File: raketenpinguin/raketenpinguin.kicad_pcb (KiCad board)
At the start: 2 copper layers, 44.3 x 88 mm, 6 parts, among them J101 Conn_01x01_Male, J102 Conn_01x01_Male

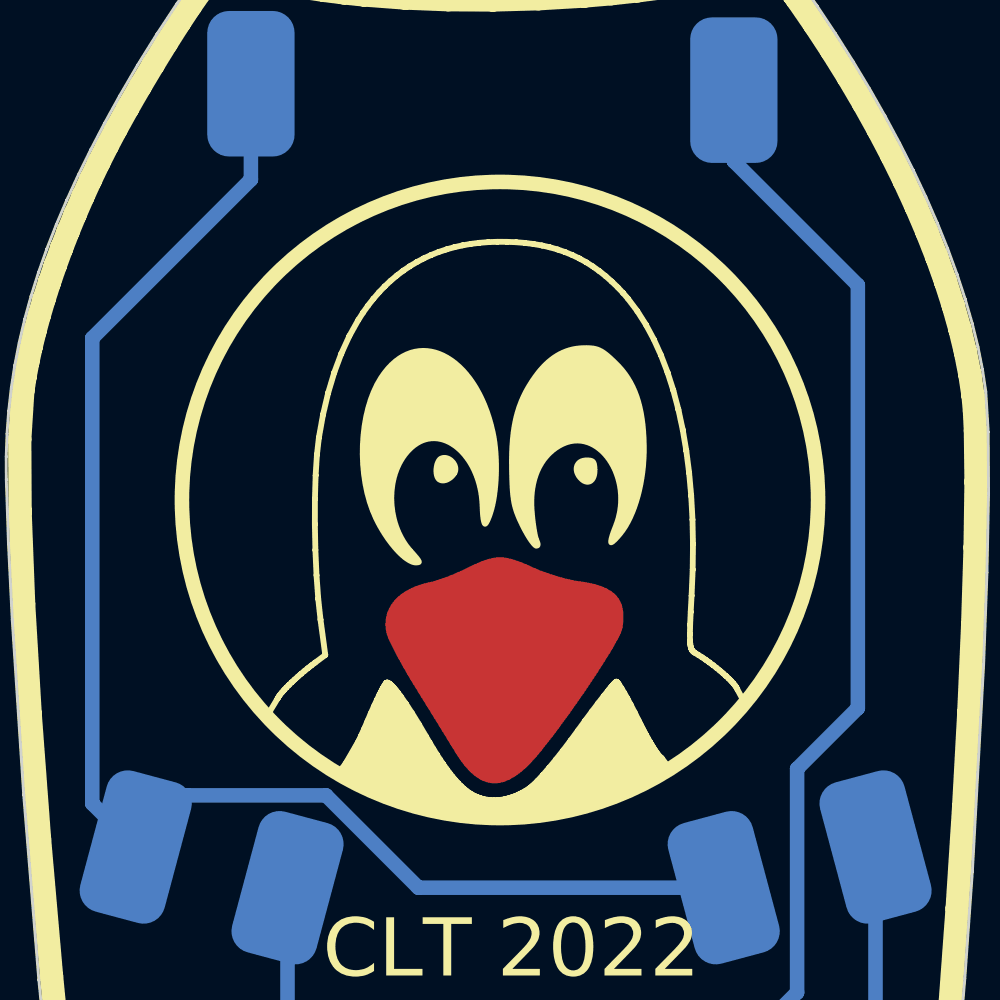
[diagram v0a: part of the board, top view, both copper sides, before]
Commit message: Raketenpinguin: Add Cu behind head
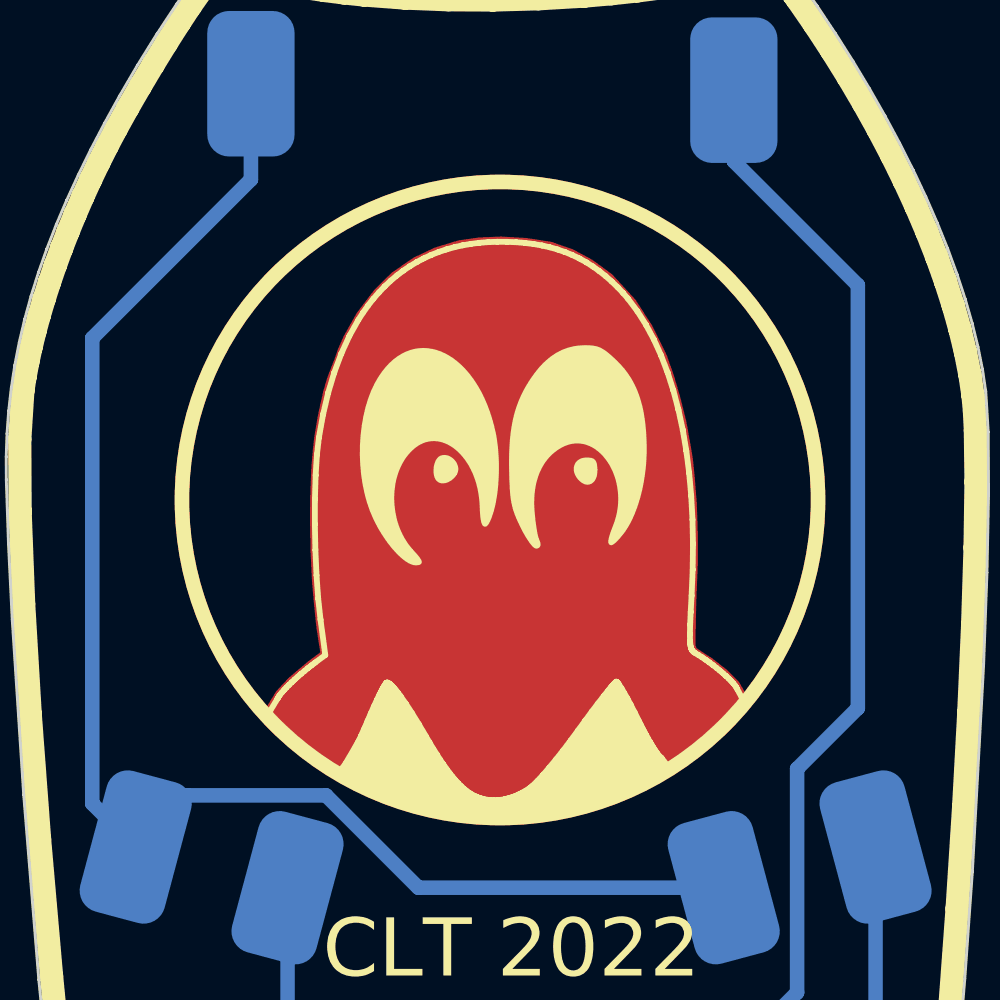
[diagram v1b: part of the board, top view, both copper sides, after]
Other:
- board text added: "Logo: Chemnitzer Linuxtage Design: CC-BY-SA Chrissi^ https://gitli.stratum0.org/chrissi/clt-soldering V2"
- board text removed: "Logo: Chemnitzer Linuxtage Design: CC-BY-SA Chrissi^ https://gitli.stratum0.org/chrissi/clt-soldering"
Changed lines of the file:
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@@
     (48 "B.Fab" user)
     (49 "F.Fab" user)
-    (50 "User.1" user)
-    (51 "User.2" user)
-    (52 "User.3" user)
-    (53 "User.4" user)
-    (54 "User.5" user)
-    (55 "User.6" user)
-    (56 "User.7" user)
-    (57 "User.8" user)
-    (58 "User.9" user)
+    (50 "User.1" user "Nutzer.1")
+    (51 "User.2" user "Nutzer.2")
+    (52 "User.3" user "Nutzer.3")
+    (53 "User.4" user "Nutzer.4")
+    (54 "User.5" user "Nutzer.5")
+    (55 "User.6" user "Nutzer.6")
+    (56 "User.7" user "Nutzer.7")
+    (57 "User.8" user "Nutzer.8")
+    (58 "User.9" user "Nutzer.9")
   )
   (setup
@@
     )
     (pad_to_mask_clearance 0)
-    (grid_origin 101.69 51.08)
+    (grid_origin 90.27 57.12)
     (pcbplotparams
       (layerselection 0x00010fc_ffffffff)
@@
       (drillshape 0)
       (scaleselection 1)
-      (outputdirectory "V1/drill/")
+      (outputdirectory "V2/drill")
     )
   )
@@
       (net 4 "/GND") (pintype "passive"))
   )
+  (gr_circle (center 79.096742 57.26) (end 90.023484 57.26) (layer "F.Cu") (width 0.5) (fill none))
   (gr_poly
     (pts
@@
       (xy 80.058218 66.301112)
     ) (layer "F.Cu") (width 0.126504) (fill solid))
+  (gr_poly
+    (pts
+      (xy 80 48.36)
+      (xy 80.84 48.49)
+      (xy 81.56 48.74)
+      (xy 82.21 49.09)
+      (xy 82.88 49.58)
+      (xy 83.68 50.45)
+      (xy 84.25 51.34)
+      (xy 84.74 52.34)
+      (xy 84.99 53.06)
+      (xy 85.21 53.82)
+      (xy 85.4 54.58)
+      (xy 85.53 55.31)
+      (xy 85.62 55.83)
+      (xy 85.69 56.52)
+      (xy 85.76 57.41)
+      (xy 85.79 58.36)
+      (xy 85.79 59.49)
+      (xy 85.74 60.77)
+      (xy 85.72 61.69)
+      (xy 85.71 62.24)
+      (xy 85.76 62.41)
+      (xy 86.34 62.79)
+      (xy 86.85 63.19)
+      (xy 87.22 63.56)
+      (xy 87.44 63.94)
+      (xy 86.74 64.73)
+      (xy 86.1 65.34)
+      (xy 85.09 66.11)
+      (xy 83.71 66.95)
+      (xy 82.11 67.66)
+      (xy 80.54 68.06)
+      (xy 78.41 68.13)
+      (xy 76.33 67.76)
+      (xy 74.94 67.31)
+      (xy 73.59 66.4)
+      (xy 72.86 65.94)
+      (xy 71.97 65.25)
+      (xy 71.14 64.48)
+      (xy 71.16 64.43)
+      (xy 71.49 63.89)
+      (xy 71.92 63.43)
+      (xy 72.56 62.89)
+      (xy 73.03 62.54)
+      (xy 72.89 61.64)
+      (xy 72.81 60.87)
+      (xy 72.74 60.08)
+      (xy 72.69 59.07)
+      (xy 72.67 58.08)
+      (xy 72.67 57.61)
+      (xy 72.68 57.08)
+      (xy 72.7 56.52)
+      (xy 72.72 56.08)
+      (xy 72.77 55.51)
+      (xy 72.82 55.08)
+      (xy 72.92 54.48)
+      (xy 73 54.09)
+      (xy 73.13 53.52)
+      (xy 73.26 53.08)
+      (xy 73.49 52.49)
+      (xy 73.63 52.1)
+      (xy 73.82 51.67)
+      (xy 74.26 50.89)
+      (xy 74.86 50.1)
+      (xy 75.43 49.54)
+      (xy 76.16 49.03)
+      (xy 76.9 48.68)
+      (xy 77.69 48.44)
+      (xy 78.4 48.34)
+      (xy 79.14 48.31)
+    ) (layer "F.Cu") (width 0.2) (fill solid))
   (gr_poly
     (pts
@@
     (effects (font (size 1 1) (thickness 0.15)) (justify mirror))
   )
-  (gr_text "Logo: Chemnitzer Linuxtage\nDesign: CC-BY-SA Chrissi^\nhttps://gitli.stratum0.org/chrissi/clt-soldering" (at 79.19 116.78 90) (layer "B.SilkS")
+  (gr_text "Logo: Chemnitzer Linuxtage\nDesign: CC-BY-SA Chrissi^\nhttps://gitli.stratum0.org/chrissi/clt-soldering\nV2" (at 79.19 116.78 90) (layer "B.SilkS")
     (effects (font (size 1 1) (thickness 0.15)) (justify right mirror))
   )
